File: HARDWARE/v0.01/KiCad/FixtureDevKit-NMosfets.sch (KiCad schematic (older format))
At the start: 32 parts

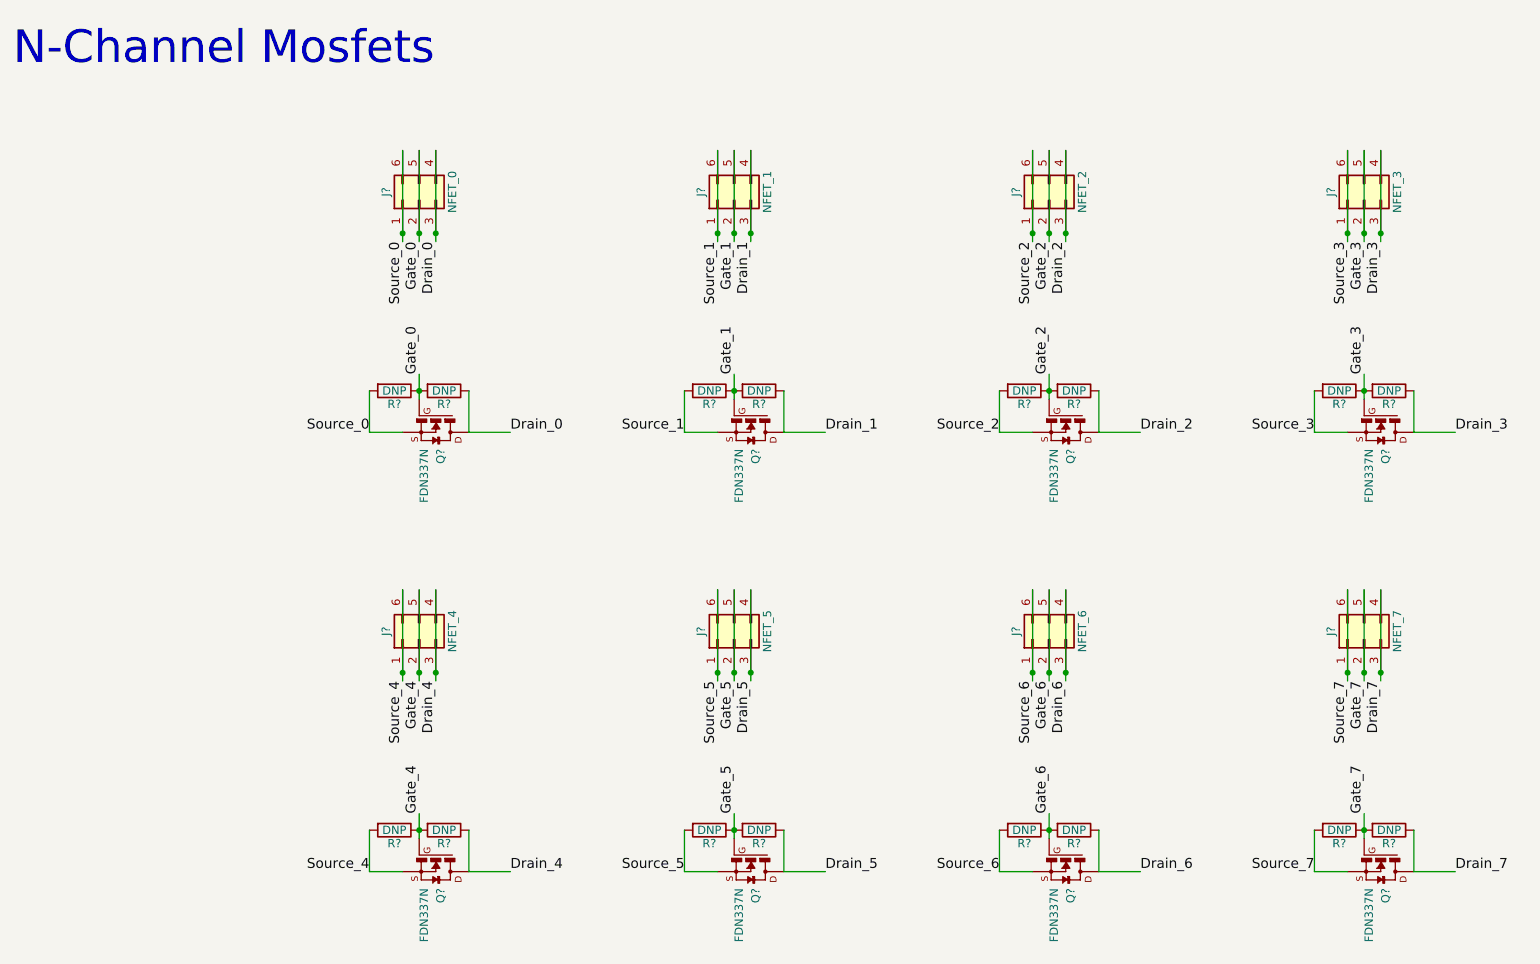
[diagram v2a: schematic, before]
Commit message: adjusting page sizes and cleaning up schematics
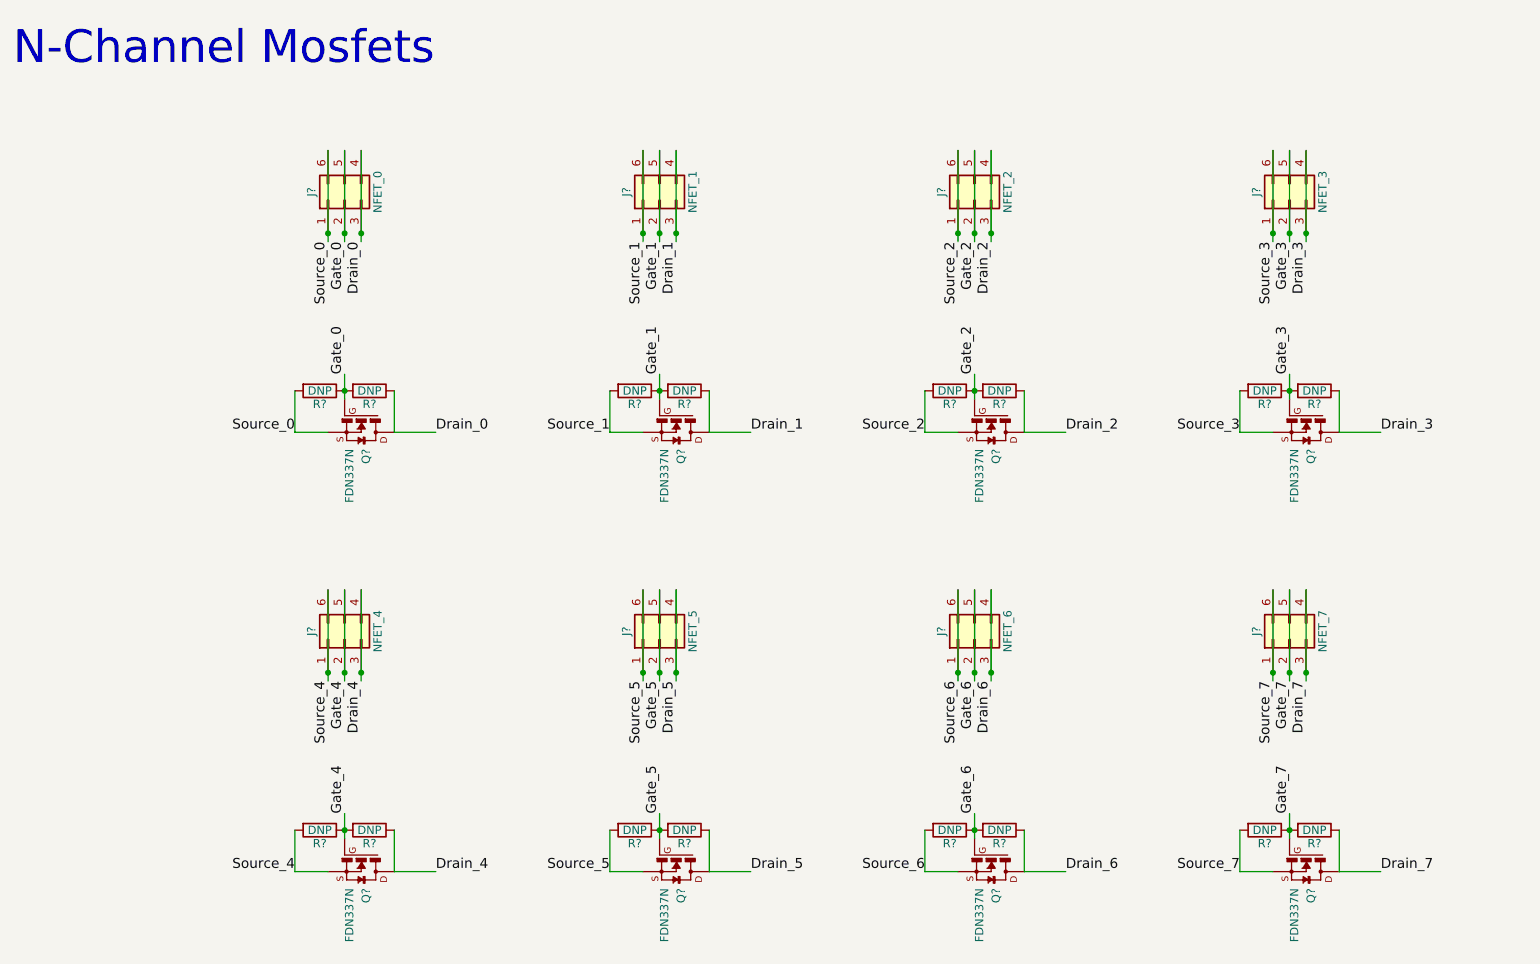
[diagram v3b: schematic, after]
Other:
- moved on the sheet: J?, Q?, R?

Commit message: cleaning up schematic, run rules check, generate net list
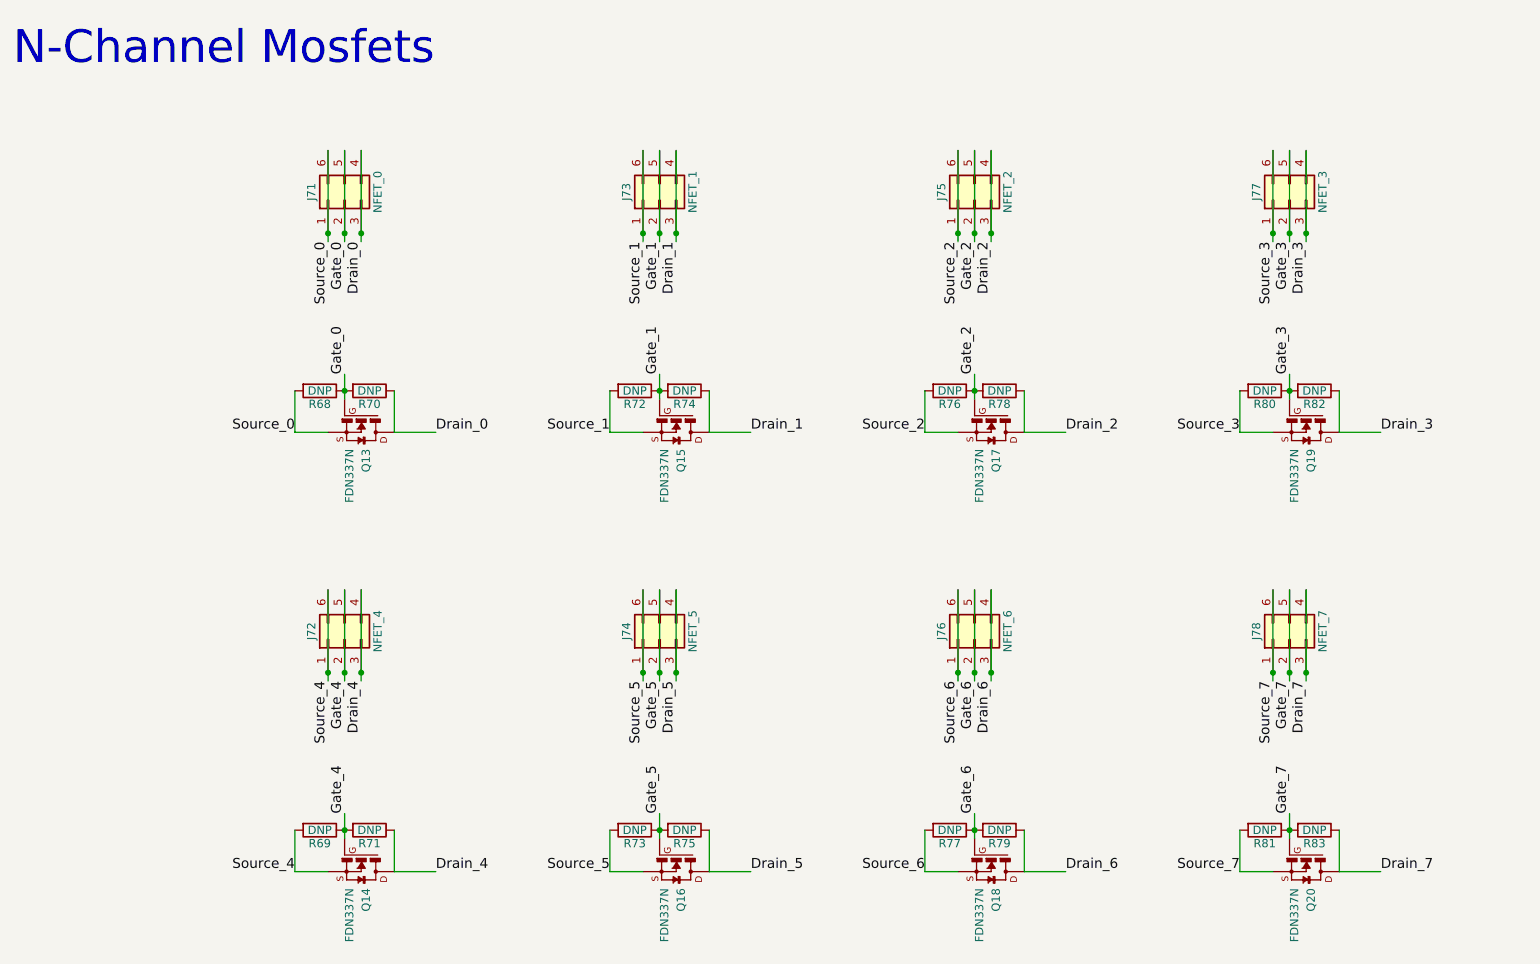
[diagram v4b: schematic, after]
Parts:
- gave numbers to parts that had none: 32
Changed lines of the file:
@@
 N-Channel Mosfets
 $Comp
-L Conn_02x03_Counter_Clockwise J?
+L Conn_02x03_Counter_Clockwise J71
 U 1 1 59F0D8BC
 P 2500 1550
-F 0 "J?" H 2550 1750 50  0000 C CNN
+F 0 "J71" H 2550 1750 50  0000 C CNN
 F 1 "NFET_0" H 2550 1350 50  0000 C CNN
 F 2 "" H 2500 1550 50  0001 C CNN
@@
 Drain_0
 $Comp
-L FDN337N Q?
+L FDN337N Q13
 U 1 1 59F0D7B8
 P 2600 2950
-F 0 "Q?" H 2700 2950 50  0000 L BNN
+F 0 "Q13" H 2700 2950 50  0000 L BNN
 F 1 "FDN337N" H 2700 2850 50  0000 L BNN
 F 2 "SSOT-3" H 2600 2950 50  0001 L BNN
@@
 	2200 2700 2200 2950
 $Comp
-L R R?
+L R R68
 U 1 1 59F0DB1F
 P 2350 2700
-F 0 "R?" V 2430 2700 50  0000 C CNN
+F 0 "R68" V 2430 2700 50  0000 C CNN
 F 1 "DNP" V 2350 2700 50  0000 C CNN
 F 2 "" V 2280 2700 50  0001 C CNN
@@
 	2800 2700 2800 2950
 $Comp
-L R R?
+L R R70
 U 1 1 59F0DAD5
 P 2650 2700
-F 0 "R?" V 2730 2700 50  0000 C CNN
+F 0 "R70" V 2730 2700 50  0000 C CNN
 F 1 "DNP" V 2650 2700 50  0000 C CNN
 F 2 "" V 2580 2700 50  0001 C CNN
@@
 	2500 5250 2500 5400
 $Comp
-L R R?
+L R R69
 U 1 1 59F0F7B7
 P 2350 5350
-F 0 "R?" V 2430 5350 50  0000 C CNN
+F 0 "R69" V 2430 5350 50  0000 C CNN
 F 1 "DNP" V 2350 5350 50  0000 C CNN
 F 2 "" V 2280 5350 50  0001 C CNN
@@
 $EndComp
 $Comp
-L R R?
+L R R71
 U 1 1 59F0F7B1
 P 2650 5350
-F 0 "R?" V 2730 5350 50  0000 C CNN
+F 0 "R71" V 2730 5350 50  0000 C CNN
 F 1 "DNP" V 2650 5350 50  0000 C CNN
 F 2 "" V 2580 5350 50  0001 C CNN
@@
 Source_4
 $Comp
-L Conn_02x03_Counter_Clockwise J?
+L Conn_02x03_Counter_Clockwise J72
 U 1 1 59F0F7A5
 P 2500 4200
-F 0 "J?" H 2550 4400 50  0000 C CNN
+F 0 "J72" H 2550 4400 50  0000 C CNN
 F 1 "NFET_4" H 2550 4000 50  0000 C CNN
 F 2 "" H 2500 4200 50  0001 C CNN
@@
 $EndComp
 $Comp
-L FDN337N Q?
+L FDN337N Q14
 U 1 1 59F0F79F
 P 2600 5600
-F 0 "Q?" H 2700 5600 50  0000 L BNN
+F 0 "Q14" H 2700 5600 50  0000 L BNN
 F 1 "FDN337N" H 2700 5500 50  0000 L BNN
 F 2 "SSOT-3" H 2600 5600 50  0001 L BNN
@@
 	8200 5250 8200 5400
 $Comp
-L R R?
+L R R81
 U 1 1 59F0F838
 P 8050 5350
-F 0 "R?" V 8130 5350 50  0000 C CNN
+F 0 "R81" V 8130 5350 50  0000 C CNN
 F 1 "DNP" V 8050 5350 50  0000 C CNN
 F 2 "" V 7980 5350 50  0001 C CNN
@@
 $EndComp
 $Comp
-L R R?
+L R R83
 U 1 1 59F0F832
 P 8350 5350
-F 0 "R?" V 8430 5350 50  0000 C CNN
+F 0 "R83" V 8430 5350 50  0000 C CNN
 F 1 "DNP" V 8350 5350 50  0000 C CNN
 F 2 "" V 8280 5350 50  0001 C CNN
@@
 Source_7
 $Comp
-L Conn_02x03_Counter_Clockwise J?
+L Conn_02x03_Counter_Clockwise J78
 U 1 1 59F0F826
 P 8200 4200
-F 0 "J?" H 8250 4400 50  0000 C CNN
+F 0 "J78" H 8250 4400 50  0000 C CNN
 F 1 "NFET_7" H 8250 4000 50  0000 C CNN
 F 2 "" H 8200 4200 50  0001 C CNN
@@
 $EndComp
 $Comp
-L FDN337N Q?
+L FDN337N Q20
 U 1 1 59F0F820
 P 8300 5600
-F 0 "Q?" H 8400 5600 50  0000 L BNN
+F 0 "Q20" H 8400 5600 50  0000 L BNN
 F 1 "FDN337N" H 8400 5500 50  0000 L BNN
 F 2 "SSOT-3" H 8300 5600 50  0001 L BNN
@@
 	6300 5250 6300 5400
 $Comp
-L R R?
+L R R77
 U 1 1 59F0F80D
 P 6150 5350
-F 0 "R?" V 6230 5350 50  0000 C CNN
+F 0 "R77" V 6230 5350 50  0000 C CNN
 F 1 "DNP" V 6150 5350 50  0000 C CNN
 F 2 "" V 6080 5350 50  0001 C CNN
@@
 $EndComp
 $Comp
-L R R?
+L R R79
 U 1 1 59F0F807
 P 6450 5350
-F 0 "R?" V 6530 5350 50  0000 C CNN
+F 0 "R79" V 6530 5350 50  0000 C CNN
 F 1 "DNP" V 6450 5350 50  0000 C CNN
 F 2 "" V 6380 5350 50  0001 C CNN
@@
 Source_6
 $Comp
-L Conn_02x03_Counter_Clockwise J?
+L Conn_02x03_Counter_Clockwise J76
 U 1 1 59F0F7FB
 P 6300 4200
-F 0 "J?" H 6350 4400 50  0000 C CNN
+F 0 "J76" H 6350 4400 50  0000 C CNN
 F 1 "NFET_6" H 6350 4000 50  0000 C CNN
 F 2 "" H 6300 4200 50  0001 C CNN
@@
 $EndComp
 $Comp
-L FDN337N Q?
+L FDN337N Q18
 U 1 1 59F0F7F5
 P 6400 5600
-F 0 "Q?" H 6500 5600 50  0000 L BNN
+F 0 "Q18" H 6500 5600 50  0000 L BNN
 F 1 "FDN337N" H 6500 5500 50  0000 L BNN
 F 2 "SSOT-3" H 6400 5600 50  0001 L BNN
@@
 	4400 5250 4400 5400
 $Comp
-L R R?
+L R R73
 U 1 1 59F0F7E2
 P 4250 5350
-F 0 "R?" V 4330 5350 50  0000 C CNN
+F 0 "R73" V 4330 5350 50  0000 C CNN
 F 1 "DNP" V 4250 5350 50  0000 C CNN
 F 2 "" V 4180 5350 50  0001 C CNN
@@
 $EndComp
 $Comp
-L R R?
+L R R75
 U 1 1 59F0F7DC
 P 4550 5350
-F 0 "R?" V 4630 5350 50  0000 C CNN
+F 0 "R75" V 4630 5350 50  0000 C CNN
 F 1 "DNP" V 4550 5350 50  0000 C CNN
 F 2 "" V 4480 5350 50  0001 C CNN
@@
 Source_5
 $Comp
-L Conn_02x03_Counter_Clockwise J?
+L Conn_02x03_Counter_Clockwise J74
 U 1 1 59F0F7D0
 P 4400 4200
-F 0 "J?" H 4450 4400 50  0000 C CNN
+F 0 "J74" H 4450 4400 50  0000 C CNN
 F 1 "NFET_5" H 4450 4000 50  0000 C CNN
 F 2 "" H 4400 4200 50  0001 C CNN
@@
 $EndComp
 $Comp
-L FDN337N Q?
+L FDN337N Q16
 U 1 1 59F0F7CA
 P 4500 5600
-F 0 "Q?" H 4600 5600 50  0000 L BNN
+F 0 "Q16" H 4600 5600 50  0000 L BNN
 F 1 "FDN337N" H 4600 5500 50  0000 L BNN
 F 2 "SSOT-3" H 4500 5600 50  0001 L BNN
@@
 	8200 2600 8200 2750
 $Comp
-L R R?
+L R R80
 U 1 1 59F0E6B4
 P 8050 2700
-F 0 "R?" V 8130 2700 50  0000 C CNN
+F 0 "R80" V 8130 2700 50  0000 C CNN
 F 1 "DNP" V 8050 2700 50  0000 C CNN
 F 2 "" V 7980 2700 50  0001 C CNN
@@
 $EndComp
 $Comp
-L R R?
+L R R82
 U 1 1 59F0E6AE
 P 8350 2700
-F 0 "R?" V 8430 2700 50  0000 C CNN
+F 0 "R82" V 8430 2700 50  0000 C CNN
 F 1 "DNP" V 8350 2700 50  0000 C CNN
 F 2 "" V 8280 2700 50  0001 C CNN
@@
 Source_3
 $Comp
-L Conn_02x03_Counter_Clockwise J?
+L Conn_02x03_Counter_Clockwise J77
 U 1 1 59F0E6A2
 P 8200 1550
-F 0 "J?" H 8250 1750 50  0000 C CNN
+F 0 "J77" H 8250 1750 50  0000 C CNN
 F 1 "NFET_3" H 8250 1350 50  0000 C CNN
 F 2 "" H 8200 1550 50  0001 C CNN
@@
 $EndComp
 $Comp
-L FDN337N Q?
+L FDN337N Q19
 U 1 1 59F0E69C
 P 8300 2950
-F 0 "Q?" H 8400 2950 50  0000 L BNN
+F 0 "Q19" H 8400 2950 50  0000 L BNN
 F 1 "FDN337N" H 8400 2850 50  0000 L BNN
 F 2 "SSOT-3" H 8300 2950 50  0001 L BNN
@@
 	6300 2600 6300 2750
 $Comp
-L R R?
+L R R76
 U 1 1 59F0E689
 P 6150 2700
-F 0 "R?" V 6230 2700 50  0000 C CNN
+F 0 "R76" V 6230 2700 50  0000 C CNN
 F 1 "DNP" V 6150 2700 50  0000 C CNN
 F 2 "" V 6080 2700 50  0001 C CNN
@@
 $EndComp
 $Comp
-L R R?
+L R R78
 U 1 1 59F0E683
 P 6450 2700
-F 0 "R?" V 6530 2700 50  0000 C CNN
+F 0 "R78" V 6530 2700 50  0000 C CNN
 F 1 "DNP" V 6450 2700 50  0000 C CNN
 F 2 "" V 6380 2700 50  0001 C CNN
@@
 Source_2
 $Comp
-L Conn_02x03_Counter_Clockwise J?
+L Conn_02x03_Counter_Clockwise J75
 U 1 1 59F0E677
 P 6300 1550
-F 0 "J?" H 6350 1750 50  0000 C CNN
+F 0 "J75" H 6350 1750 50  0000 C CNN
 F 1 "NFET_2" H 6350 1350 50  0000 C CNN
 F 2 "" H 6300 1550 50  0001 C CNN
@@
 $EndComp
 $Comp
-L FDN337N Q?
+L FDN337N Q17
 U 1 1 59F0E671
 P 6400 2950
-F 0 "Q?" H 6500 2950 50  0000 L BNN
+F 0 "Q17" H 6500 2950 50  0000 L BNN
 F 1 "FDN337N" H 6500 2850 50  0000 L BNN
 F 2 "SSOT-3" H 6400 2950 50  0001 L BNN
@@
 	4400 2600 4400 2750
 $Comp
-L R R?
+L R R72
 U 1 1 59F0E10A
 P 4250 2700
-F 0 "R?" V 4330 2700 50  0000 C CNN
+F 0 "R72" V 4330 2700 50  0000 C CNN
 F 1 "DNP" V 4250 2700 50  0000 C CNN
 F 2 "" V 4180 2700 50  0001 C CNN
@@
 $EndComp
 $Comp
-L R R?
+L R R74
 U 1 1 59F0E104
 P 4550 2700
-F 0 "R?" V 4630 2700 50  0000 C CNN
+F 0 "R74" V 4630 2700 50  0000 C CNN
 F 1 "DNP" V 4550 2700 50  0000 C CNN
 F 2 "" V 4480 2700 50  0001 C CNN
@@
 Source_1
 $Comp
-L Conn_02x03_Counter_Clockwise J?
+L Conn_02x03_Counter_Clockwise J73
 U 1 1 59F0E0F8
 P 4400 1550
-F 0 "J?" H 4450 1750 50  0000 C CNN
+F 0 "J73" H 4450 1750 50  0000 C CNN
 F 1 "NFET_1" H 4450 1350 50  0000 C CNN
 F 2 "" H 4400 1550 50  0001 C CNN
@@
 $EndComp
 $Comp
-L FDN337N Q?
+L FDN337N Q15
 U 1 1 59F0E0F2
 P 4500 2950
-F 0 "Q?" H 4600 2950 50  0000 L BNN
+F 0 "Q15" H 4600 2950 50  0000 L BNN
 F 1 "FDN337N" H 4600 2850 50  0000 L BNN
 F 2 "SSOT-3" H 4500 2950 50  0001 L BNN
